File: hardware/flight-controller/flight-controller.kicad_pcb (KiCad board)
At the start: 4 copper layers, 66.7 x 75.4 mm, 134 parts, among them J1 XT-60, J10 IDC-10, J2 Conn_01x05, J3 IDC-10, J4 Conn_01x03, J5 Conn_01x03, J6 Conn_01x03, J7 IDC-10, J8 XT-60, J9 Conn_01x03, Q1 IRFR5305, Q2 S8550, SW1 JS102011SAQN, SW2 KMS231GPLFS, U1 INA226, U2 LM1117MP-3.3, U3 LV14340, U4 ESP-12E, U5 STM32U535RET6, U6 HMC5883L, U7 MPU-6050, U8 BMP280, U9 HX711, Y1 8MHz

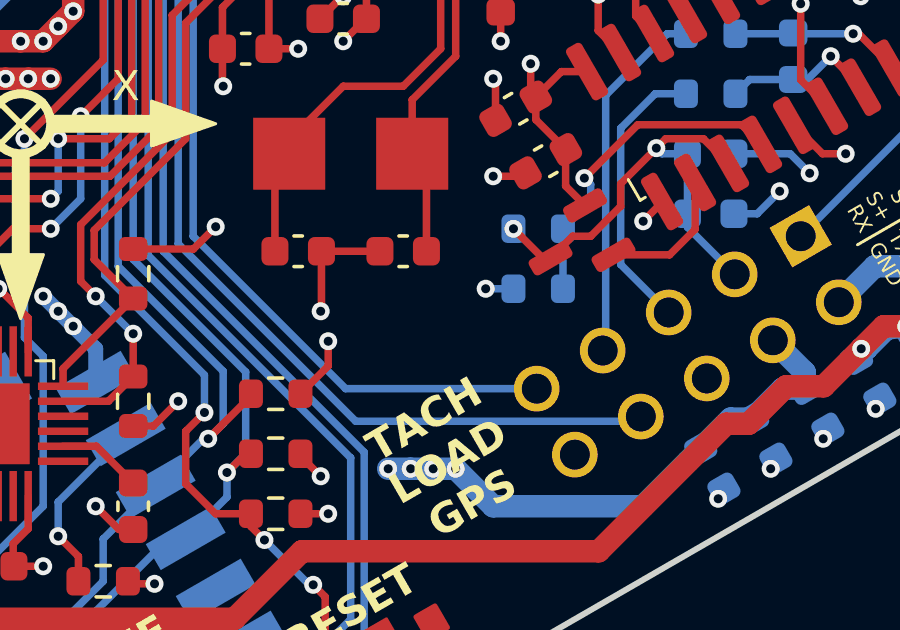
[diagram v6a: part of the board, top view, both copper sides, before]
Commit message: fix connector GPS pinout, update AUX pinouts
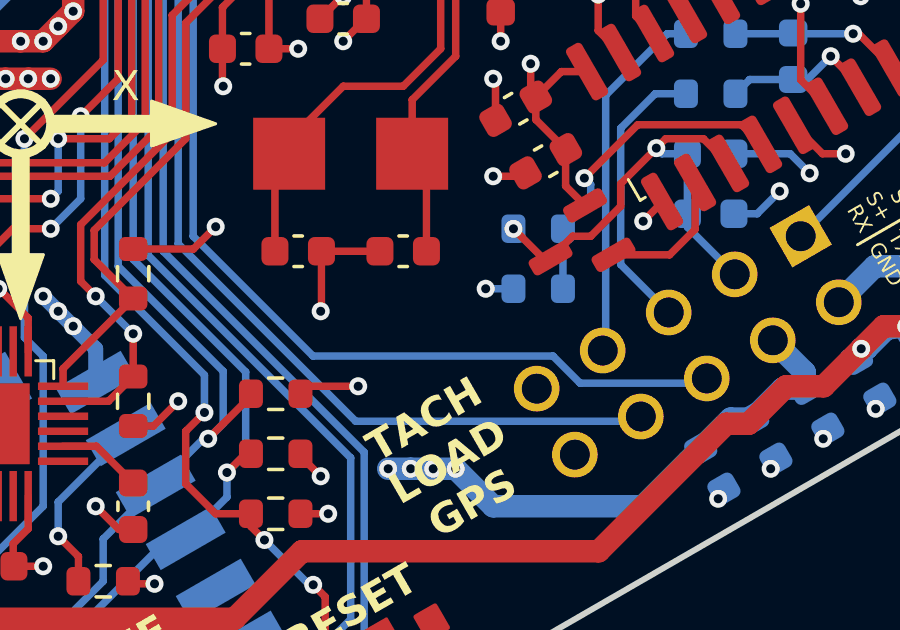
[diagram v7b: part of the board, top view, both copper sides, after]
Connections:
- J10 pad 6: GND -> GPS_TXD
- J10 pad 9: GPS_TXD -> GND
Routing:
- net GPS_TXD: track 31.1 -> 36.9 mm
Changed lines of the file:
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@@
 			(layers "*.Cu" "*.Mask")
 			(remove_unused_layers no)
-			(net 1 "GND")
+			(net 52 "GPS_TXD")
 			(pinfunction "Pin_6")
 			(pintype "passive")
@@
 			(layers "*.Cu" "*.Mask")
 			(remove_unused_layers no)
-			(net 52 "GPS_TXD")
+			(net 1 "GND")
 			(pinfunction "Pin_9")
 			(pintype "passive")
@@
 	)
 	(segment
-		(start 172.53154 116.167)
-		(end 172.688835 116.009705)
-		(width 0.25)
-		(layer "B.Cu")
-		(net 1)
-	)
-	(segment
 		(start 151.25 114.5)
 		(end 150.75 114)
@@
 	)
 	(segment
+		(start 160.75 116.5)
+		(end 159.075 116.5)
+		(width 0.25)
+		(layer "F.Cu")
+		(net 2)
+	)
+	(segment
 		(start 146.087502 117.000001)
 		(end 144.883887 117.000001)
@@
 	)
 	(segment
-		(start 159.75 115.825)
-		(end 158.825 116.75)
-		(width 0.25)
-		(layer "F.Cu")
-		(net 2)
-	)
-	(segment
 		(start 137 107.75)
 		(end 136.975 107.775)
@@
 	)
 	(segment
-		(start 136.975 107.775)
-		(end 136.975 108.75)
+		(start 159.075 116.5)
+		(end 158.825 116.75)
 		(width 0.25)
 		(layer "F.Cu")
@@
 	)
 	(segment
-		(start 158.75 105.25)
-		(end 157.775 105.25)
+		(start 136.975 107.775)
+		(end 136.975 108.75)
 		(width 0.25)
 		(layer "F.Cu")
@@
 	)
 	(segment
-		(start 159.75 115)
-		(end 159.75 115.825)
+		(start 158.75 105.25)
+		(end 157.775 105.25)
 		(width 0.25)
 		(layer "F.Cu")
@@
 	)
 	(via
-		(at 159.75 115)
+		(at 160.75 116.5)
 		(size 0.6)
 		(drill 0.3)
@@
 	)
 	(segment
+		(start 172.53154 116.167)
+		(end 172.688835 116.009705)
+		(width 0.25)
+		(layer "B.Cu")
+		(net 52)
+	)
+	(segment
+		(start 167.243 115.493)
+		(end 168.147 116.397)
+		(width 0.25)
+		(layer "B.Cu")
+		(net 52)
+	)
+	(segment
+		(start 172.213296 116.397)
+		(end 172.370591 116.239705)
+		(width 0.25)
+		(layer "B.Cu")
+		(net 52)
+	)
+	(segment
+		(start 155.25 102.25)
+		(end 155.25 111.5)
+		(width 0.25)
+		(layer "B.Cu")
+		(net 52)
+	)
+	(segment
 		(start 157 100.5)
 		(end 155.25 102.25)
@@
 	)
 	(segment
-		(start 158 98.5)
-		(end 157 99.5)
+		(start 168.147 116.397)
+		(end 172.213296 116.397)
 		(width 0.25)
 		(layer "B.Cu")
@@
 	)
 	(segment
-		(start 157 99.5)
-		(end 157 100.5)
+		(start 155.25 111.5)
+		(end 159.243 115.493)
 		(width 0.25)
 		(layer "B.Cu")
@@
 	)
 	(segment
-		(start 155.25 111.5)
-		(end 160.33 116.58)
+		(start 157 99.5)
+		(end 157 100.5)
 		(width 0.25)
 		(layer "B.Cu")
@@
 	)
 	(segment
-		(start 160.33 116.58)
-		(end 166.701182 116.58)
+		(start 159.243 115.493)
+		(end 167.243 115.493)
 		(width 0.25)
 		(layer "B.Cu")
@@
 	)
 	(segment
-		(start 155.25 102.25)
-		(end 155.25 111.5)
+		(start 158 98.5)
+		(end 157 99.5)
 		(width 0.25)
 		(layer "B.Cu")
